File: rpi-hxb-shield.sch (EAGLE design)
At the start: 33 parts, among them Q1 CRYSTALX22, U2 24LC32A/SN, X1 MICROMATCH-8

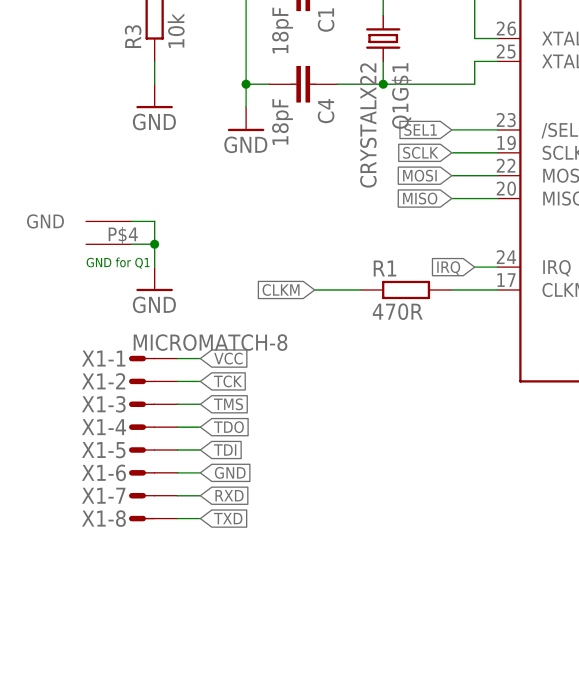
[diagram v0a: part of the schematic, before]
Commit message: removal of unneeded micromatch connector
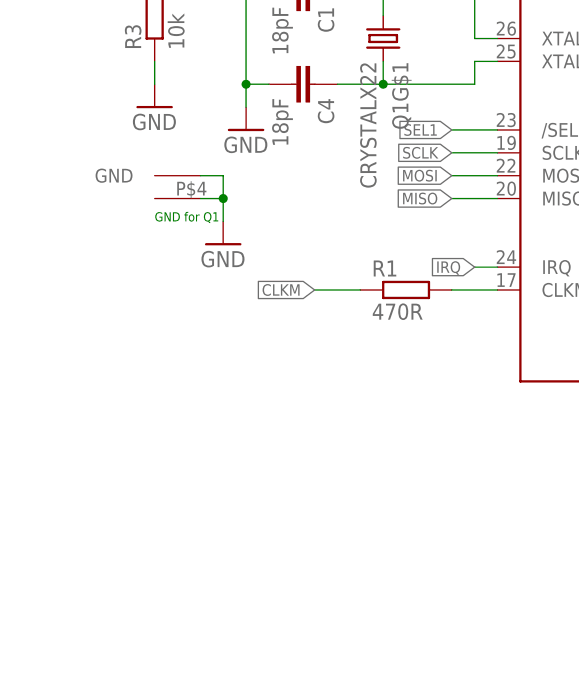
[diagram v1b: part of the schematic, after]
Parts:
- removed X1: MICROMATCH-8, con-amp-micromatch:MICROMATCH-8
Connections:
- removed net RXD: X1-7.S
- removed net TCK: X1-2.S
- removed net TDI: X1-5.S
- removed net TDO: X1-4.S
- removed net TMS: X1-3.S
- removed net TXD: X1-8.S
- net GND: no longer X1-6.S
- net VCC: no longer X1-1.S
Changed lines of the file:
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@@
 <part name="GND6" library="supply1" deviceset="GND" device=""/>
 <part name="GND7" library="supply1" deviceset="GND" device=""/>
-<part name="X1" library="con-amp-micromatch" deviceset="MICROMATCH-8" device=""/>
 <part name="GND12" library="supply1" deviceset="GND" device=""/>
 <part name="ANT1" library="discrete" deviceset="ANTENNA" device=""/>
@@
 <sheet>
 <plain>
-<text x="7.62" y="93.98" size="1.016" layer="91">GND for Q1</text>
+<text x="15.24" y="99.06" size="1.016" layer="91">GND for Q1</text>
 <text x="154.94" y="119.38" size="1.016" layer="91">wire antenna 85mm</text>
 <text x="119.38" y="43.18" size="1.016" layer="91">solder pads for antenna</text>
@@
 <instance part="GND6" gate="1" x="111.76" y="165.1" rot="R90"/>
 <instance part="GND7" gate="1" x="15.24" y="111.76"/>
-<instance part="X1" gate="-1" x="12.7" y="83.82"/>
-<instance part="X1" gate="-2" x="12.7" y="81.28"/>
-<instance part="X1" gate="-3" x="12.7" y="78.74"/>
-<instance part="X1" gate="-4" x="12.7" y="76.2"/>
-<instance part="X1" gate="-5" x="12.7" y="73.66"/>
-<instance part="X1" gate="-6" x="12.7" y="71.12"/>
-<instance part="X1" gate="-7" x="12.7" y="68.58"/>
-<instance part="X1" gate="-8" x="12.7" y="66.04"/>
 <instance part="GND12" gate="1" x="149.86" y="147.32"/>
 <instance part="ANT1" gate="A" x="160.02" y="114.3"/>
 <instance part="B1" gate="G$1" x="132.08" y="101.6" rot="R270"/>
 <instance part="GND15" gate="1" x="132.08" y="86.36"/>
-<instance part="GND16" gate="1" x="15.24" y="91.44"/>
+<instance part="GND16" gate="1" x="22.86" y="96.52"/>
 <instance part="Q1" gate="G$1" x="40.64" y="119.38" rot="R270"/>
-<instance part="Q1" gate="G$2" x="7.62" y="99.06" rot="R180"/>
+<instance part="Q1" gate="G$2" x="15.24" y="104.14" rot="R180"/>
 <instance part="C1" gate="G$1" x="33.02" y="124.46" rot="R270"/>
 <instance part="C4" gate="G$1" x="33.02" y="114.3" rot="R270"/>
@@
 </segment>
 <segment>
-<wire x1="17.78" y1="71.12" x2="20.32" y2="71.12" width="0.1524" layer="91"/>
-<label x="20.32" y="71.12" size="1.27" layer="95" xref="yes"/>
-<pinref part="X1" gate="-6" pin="S"/>
-</segment>
-<segment>
 <wire x1="119.38" y1="96.52" x2="116.84" y2="96.52" width="0.1524" layer="91"/>
 <wire x1="116.84" y1="96.52" x2="116.84" y2="88.9" width="0.1524" layer="91"/>
@@
 </segment>
 <segment>
-<wire x1="15.24" y1="93.98" x2="15.24" y2="96.52" width="0.1524" layer="91"/>
-<wire x1="15.24" y1="96.52" x2="12.7" y2="96.52" width="0.1524" layer="91"/>
-<wire x1="12.7" y1="99.06" x2="15.24" y2="99.06" width="0.1524" layer="91"/>
-<wire x1="15.24" y1="99.06" x2="15.24" y2="96.52" width="0.1524" layer="91"/>
-<junction x="15.24" y="96.52"/>
+<wire x1="22.86" y1="99.06" x2="22.86" y2="101.6" width="0.1524" layer="91"/>
+<wire x1="22.86" y1="101.6" x2="20.32" y2="101.6" width="0.1524" layer="91"/>
+<wire x1="20.32" y1="104.14" x2="22.86" y2="104.14" width="0.1524" layer="91"/>
+<wire x1="22.86" y1="104.14" x2="22.86" y2="101.6" width="0.1524" layer="91"/>
+<junction x="22.86" y="101.6"/>
 <pinref part="GND16" gate="1" pin="GND"/>
 <pinref part="Q1" gate="G$2" pin="GND1"/>
@@
 </segment>
 </net>
-<net name="RXD" class="0">
-<segment>
-<wire x1="17.78" y1="68.58" x2="20.32" y2="68.58" width="0.1524" layer="91"/>
-<label x="20.32" y="68.58" size="1.27" layer="95" xref="yes"/>
-<pinref part="X1" gate="-7" pin="S"/>
-</segment>
-</net>
-<net name="TXD" class="0">
-<segment>
-<wire x1="17.78" y1="66.04" x2="20.32" y2="66.04" width="0.1524" layer="91"/>
-<label x="20.32" y="66.04" size="1.27" layer="95" xref="yes"/>
-<pinref part="X1" gate="-8" pin="S"/>
-</segment>
-</net>
 <net name="AT_RST" class="0">
 <segment>
@@
 <wire x1="205.74" y1="78.74" x2="213.36" y2="78.74" width="0.1524" layer="91"/>
 <label x="213.36" y="78.74" size="1.27" layer="95" xref="yes"/>
-</segment>
-</net>
-<net name="TCK" class="0">
-<segment>
-<wire x1="17.78" y1="81.28" x2="20.32" y2="81.28" width="0.1524" layer="91"/>
-<label x="20.32" y="81.28" size="1.27" layer="95" xref="yes"/>
-<pinref part="X1" gate="-2" pin="S"/>
-</segment>
-</net>
-<net name="TMS" class="0">
-<segment>
-<wire x1="17.78" y1="78.74" x2="20.32" y2="78.74" width="0.1524" layer="91"/>
-<label x="20.32" y="78.74" size="1.27" layer="95" xref="yes"/>
-<pinref part="X1" gate="-3" pin="S"/>
-</segment>
-</net>
-<net name="TDO" class="0">
-<segment>
-<wire x1="17.78" y1="76.2" x2="20.32" y2="76.2" width="0.1524" layer="91"/>
-<label x="20.32" y="76.2" size="1.27" layer="95" xref="yes"/>
-<pinref part="X1" gate="-4" pin="S"/>
-</segment>
-</net>
-<net name="TDI" class="0">
-<segment>
-<wire x1="17.78" y1="73.66" x2="20.32" y2="73.66" width="0.1524" layer="91"/>
-<label x="20.32" y="73.66" size="1.27" layer="95" xref="yes"/>
-<pinref part="X1" gate="-5" pin="S"/>
 </segment>
 </net>
@@
 </segment>
 <segment>
-<wire x1="17.78" y1="83.82" x2="20.32" y2="83.82" width="0.1524" layer="91"/>
-<label x="20.32" y="83.82" size="1.27" layer="95" xref="yes"/>
-<pinref part="X1" gate="-1" pin="S"/>
-</segment>
-<segment>

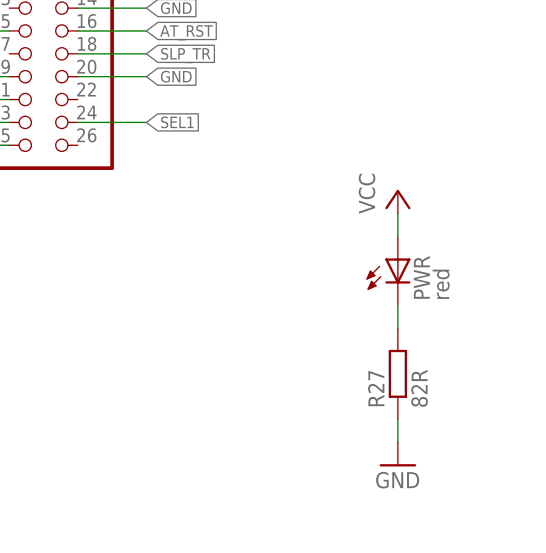
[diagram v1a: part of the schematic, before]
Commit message: removal of the power LED and ripup of all wires
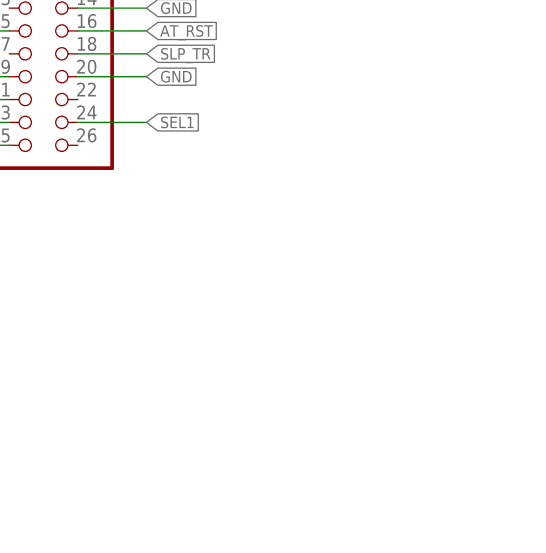
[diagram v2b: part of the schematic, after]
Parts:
- removed PWR: red, led:LEDCHIP-LED0603
- removed R27: 82R, rcl:R-EU_R0603
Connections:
- removed net N$32: PWR.C, R27.2
- net GND: no longer R27.1
- net VCC: no longer PWR.A
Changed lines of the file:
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@@
 <part name="C4" library="rcl" deviceset="C-EU" device="C0603" value="18pF"/>
 <part name="GND17" library="supply1" deviceset="GND" device=""/>
-<part name="R27" library="rcl" deviceset="R-EU_" device="R0603" value="82R"/>
-<part name="PWR" library="led" deviceset="LED" device="CHIP-LED0603" value="red"/>
-<part name="GND18" library="supply1" deviceset="GND" device=""/>
-<part name="P+4" library="supply1" deviceset="VCC" device=""/>
 <part name="P+5" library="supply1" deviceset="VCC" device=""/>
 <part name="P+8" library="supply1" deviceset="VCC" device=""/>
@@
 <instance part="C4" gate="G$1" x="33.02" y="114.3" rot="R270"/>
 <instance part="GND17" gate="1" x="25.4" y="109.22"/>
-<instance part="R27" gate="G$1" x="241.3" y="40.64" rot="R90"/>
-<instance part="PWR" gate="G$1" x="241.3" y="53.34"/>
-<instance part="GND18" gate="1" x="241.3" y="30.48"/>
-<instance part="P+4" gate="VCC" x="241.3" y="60.96"/>
 <instance part="P+5" gate="VCC" x="149.86" y="170.18"/>
 <instance part="P+8" gate="VCC" x="15.24" y="144.78"/>
@@
 </segment>
 <segment>
-<wire x1="241.3" y1="33.02" x2="241.3" y2="35.56" width="0.1524" layer="91"/>
-<pinref part="GND18" gate="1" pin="GND"/>
-<pinref part="R27" gate="G$1" pin="1"/>
-</segment>
-<segment>
 <pinref part="U2" gate="A" pin="VSS"/>
 <pinref part="GND8" gate="1" pin="GND"/>
@@
 </segment>
 </net>
-<net name="N$32" class="0">
-<segment>
-<wire x1="241.3" y1="45.72" x2="241.3" y2="48.26" width="0.1524" layer="91"/>
-<pinref part="R27" gate="G$1" pin="2"/>
-<pinref part="PWR" gate="G$1" pin="C"/>
-</segment>
-</net>
 <net name="VCC" class="0">
 <segment>
-<wire x1="241.3" y1="55.88" x2="241.3" y2="58.42" width="0.1524" layer="91"/>
-<pinref part="PWR" gate="G$1" pin="A"/>
-<pinref part="P+4" gate="VCC" pin="VCC"/>
-</segment>
-<segment>
 <wire x1="139.7" y1="162.56" x2="139.7" y2="165.1" width="0.1524" layer="91"/>

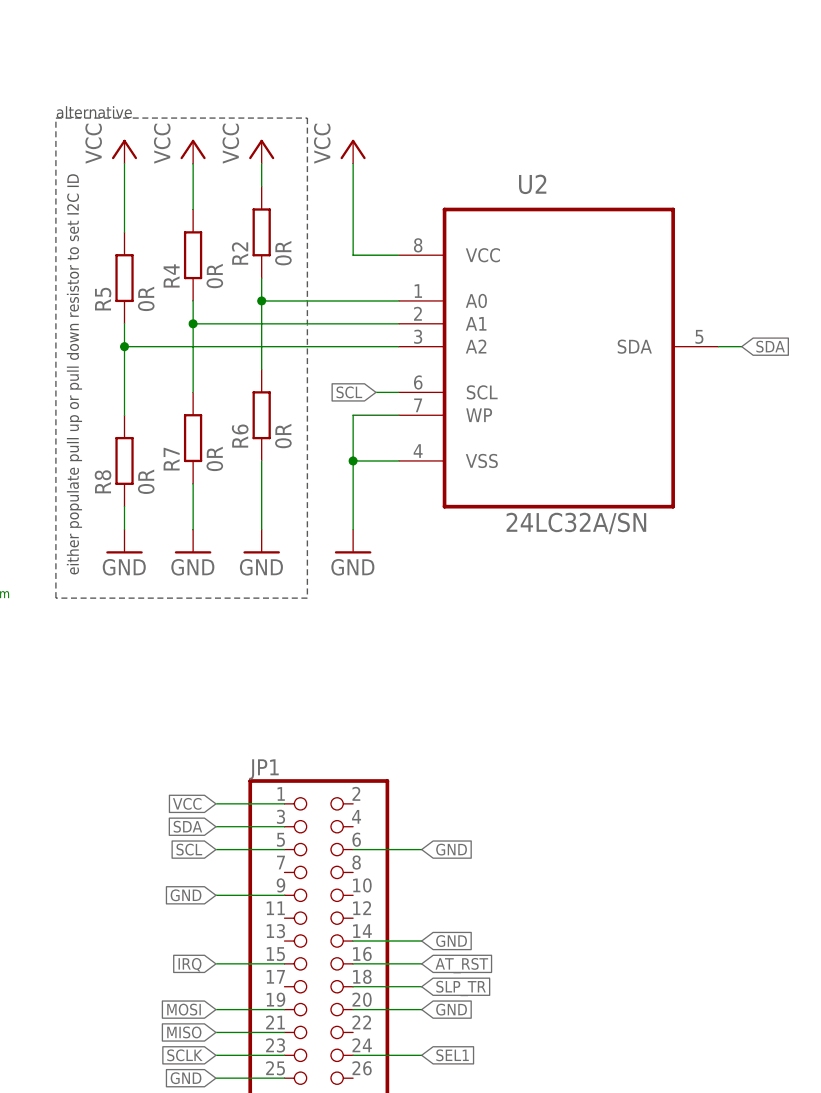
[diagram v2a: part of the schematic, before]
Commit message: swapped EEPROM to 128K variant
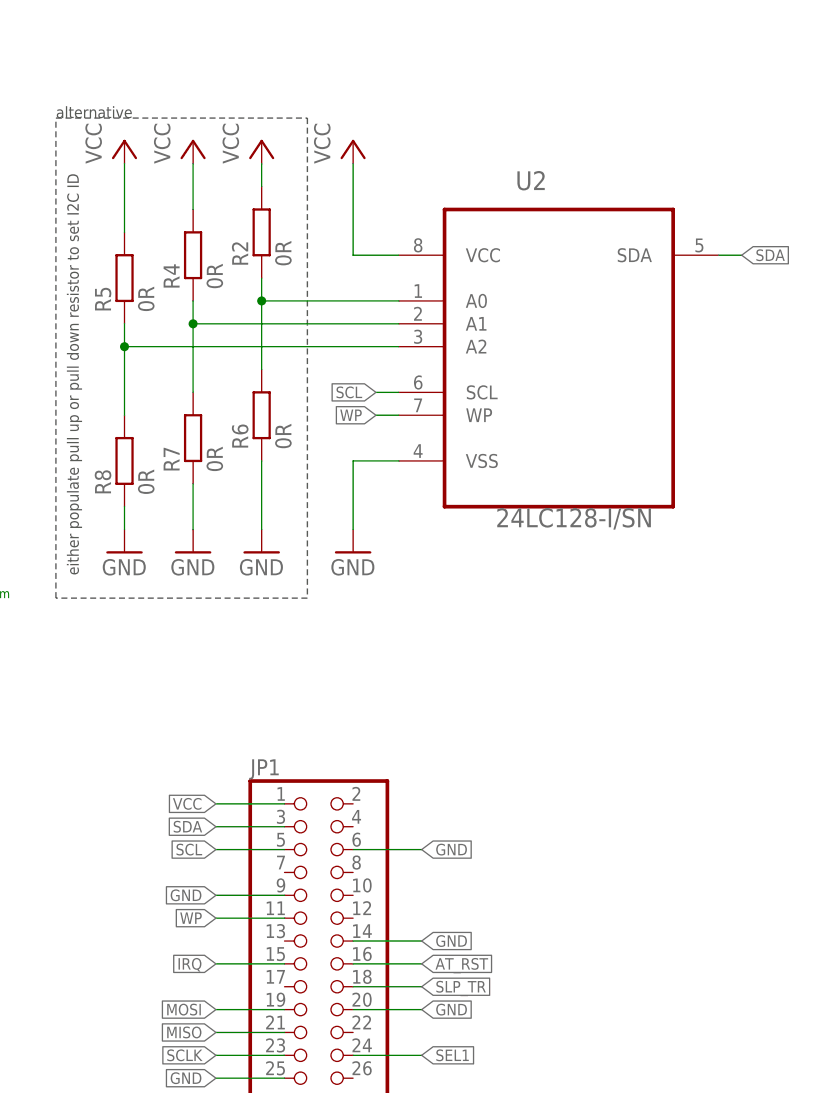
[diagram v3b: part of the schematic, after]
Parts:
- U2: value 24LC32A/SN -> 24LC128-I/SN; device hexabus:24LC32A/SN -> hexabus:24LC128-I/SN
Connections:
- new net WP: JP1.11, U2.WP
- net GND: no longer U2.WP
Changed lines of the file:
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@@
 <part name="PAD2" library="wirepad" deviceset="SMD2" device=""/>
 <part name="U$1" library="artwork" deviceset="HEXAKRAKE" device=""/>
-<part name="U2" library="hexabus" deviceset="24LC32A/SN" device=""/>
+<part name="U2" library="hexabus" deviceset="24LC128-I/SN" device=""/>
 <part name="P+1" library="supply1" deviceset="VCC" device=""/>
 <part name="GND8" library="supply1" deviceset="GND" device=""/>
@@
 <wire x1="210.82" y1="134.62" x2="205.74" y2="134.62" width="0.1524" layer="91"/>
 <wire x1="205.74" y1="134.62" x2="205.74" y2="127" width="0.1524" layer="91"/>
-<pinref part="U2" gate="A" pin="WP"/>
-<wire x1="210.82" y1="139.7" x2="205.74" y2="139.7" width="0.1524" layer="91"/>
-<wire x1="205.74" y1="139.7" x2="205.74" y2="134.62" width="0.1524" layer="91"/>
-<junction x="205.74" y="134.62"/>
 </segment>
 <segment>
@@
 <segment>
 <pinref part="U2" gate="A" pin="SDA"/>
-<wire x1="246.38" y1="147.32" x2="248.92" y2="147.32" width="0.1524" layer="91"/>
-<label x="248.92" y="147.32" size="1.27" layer="95" xref="yes"/>
+<wire x1="246.38" y1="157.48" x2="248.92" y2="157.48" width="0.1524" layer="91"/>
+<label x="248.92" y="157.48" size="1.27" layer="95" xref="yes"/>
 </segment>
 <segment>
@@
 </segment>
 </net>
+<net name="WP" class="0">
+<segment>
+<pinref part="U2" gate="A" pin="WP"/>
+<wire x1="210.82" y1="139.7" x2="208.28" y2="139.7" width="0.1524" layer="91"/>
+<label x="208.28" y="139.7" size="1.27" layer="95" rot="R180" xref="yes"/>
+</segment>
+<segment>
+<pinref part="JP1" gate="A" pin="11"/>
+<wire x1="198.12" y1="83.82" x2="190.5" y2="83.82" width="0.1524" layer="91"/>
+<label x="190.5" y="83.82" size="1.27" layer="95" rot="R180" xref="yes"/>
+</segment>
+</net>
